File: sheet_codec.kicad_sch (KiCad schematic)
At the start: 20 parts, among them J3 Carrier LEFT 1-7, J4 Carrier RIGHT 1-7, U1 ES8389, U2 TPS7A2033

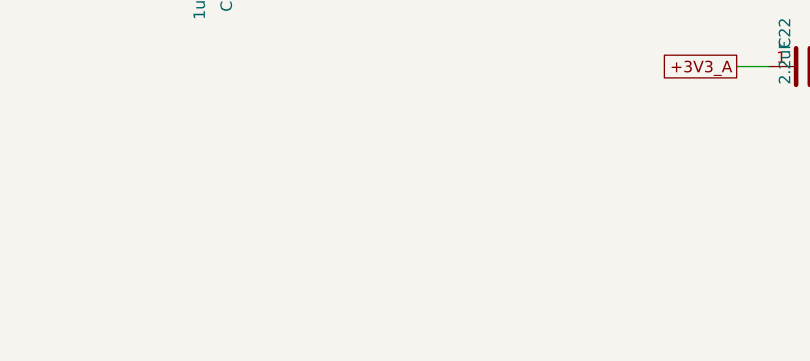
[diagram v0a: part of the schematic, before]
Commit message: codec: add J6 4-pin I2C header (3V3/AGND/SDA/SCL) for external display
- New scramble_hat:Conn_01x04 symbol + J6 in sheet_codec, connected to
  +3V3/AGND/SDA/SCL; placed on F.Cu and routed.
- Pin order (AGND/+3V3/SCL/SDA) set to match the external display's
  wiring harness.
- Fab set intentionally NOT regenerated (more design changes pending).
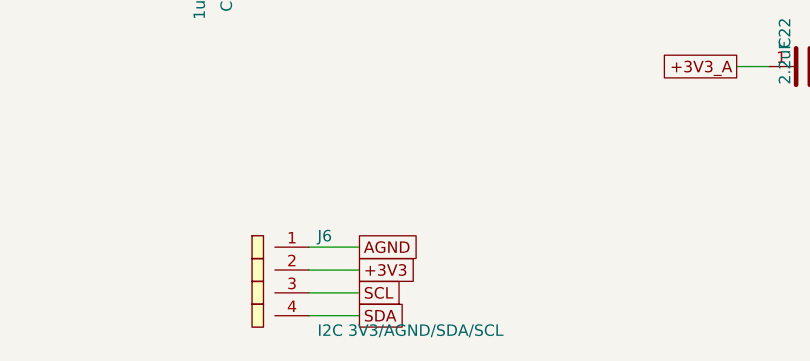
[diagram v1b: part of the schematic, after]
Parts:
- added J6: I2C 3V3/AGND/SDA/SCL, Connector_PinHeader_2.54mm:PinHeader_1x04_P2.54mm_Vertical, symbol scramble_hat:Conn_01x04
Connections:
- net +3V3: now also J6.2 (Pin_2)
- net AGND: now also J6.1 (Pin_1)
- net SCL: now also J6.3 (Pin_3)
- net SDA: now also J6.4 (Pin_4)
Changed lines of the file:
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@@
 	(wire
 		(pts
+			(xy 249.682 189.23) (xy 255.27 189.23)
+		)
+		(stroke
+			(width 0)
+			(type default)
+		)
+	)
+	(wire
+		(pts
 			(xy 299.974 117.602) (xy 309.626 117.682)
 		)
@@
 	(wire
 		(pts
+			(xy 249.682 196.85) (xy 255.27 196.85)
+		)
+		(stroke
+			(width 0)
+			(type default)
+		)
+	)
+	(wire
+		(pts
 			(xy 285.088 126.314) (xy 280.924 126.238)
 		)
@@
 	(wire
 		(pts
+			(xy 249.682 191.77) (xy 255.27 191.77)
+		)
+		(stroke
+			(width 0)
+			(type default)
+		)
+	)
+	(wire
+		(pts
 			(xy 285.088 123.774) (xy 280.924 123.698)
 		)
@@
 	(wire
 		(pts
+			(xy 249.682 194.31) (xy 255.27 194.31)
+		)
+		(stroke
+			(width 0)
+			(type default)
+		)
+	)
+	(wire
+		(pts
 			(xy 249.274 128.854) (xy 260.604 128.778)
 		)
@@
 		)
 	)
+	(global_label "SCL"
+		(shape passive)
+		(at 255.27 194.31 0)
+		(effects
+			(font
+				(size 1.27 1.27)
+			)
+			(justify left)
+		)
+		(property "Intersheetrefs" "${INTERSHEET_REFS}"
+			(at 255.27 194.31 0)
+			(hide yes)
+			(show_name no)
+			(do_not_autoplace no)
+			(effects
+				(font
+					(size 1.27 1.27)
+				)
+			)
+		)
+	)
 	(global_label "+3V3"
 		(shape passive)
@@
 		)
 	)
+	(global_label "+3V3"
+		(shape passive)
+		(at 255.27 191.77 0)
+		(effects
+			(font
+				(size 1.27 1.27)
+			)
+			(justify left)
+		)
+		(property "Intersheetrefs" "${INTERSHEET_REFS}"
+			(at 255.27 191.77 0)
+			(hide yes)
+			(show_name no)
+			(do_not_autoplace no)
+			(effects
+				(font
+					(size 1.27 1.27)
+				)
+			)
+		)
+	)
 	(global_label "+5V"
 		(shape passive)
@@
 		)
 	)
+	(global_label "SDA"
+		(shape passive)
+		(at 255.27 196.85 0)
+		(effects
+			(font
+				(size 1.27 1.27)
+			)
+			(justify left)
+		)
+		(property "Intersheetrefs" "${INTERSHEET_REFS}"
+			(at 255.27 196.85 0)
+			(hide yes)
+			(show_name no)
+			(do_not_autoplace no)
+			(effects
+				(font
+					(size 1.27 1.27)
+				)
+			)
+		)
+	)
 	(global_label "AGND"
 		(shape passive)
@@
 		)
 	)
+	(global_label "AGND"
+		(shape passive)
+		(at 255.27 189.23 0)
+		(effects
+			(font
+				(size 1.27 1.27)
+			)
+			(justify left)
+		)
+		(property "Intersheetrefs" "${INTERSHEET_REFS}"
+			(at 255.27 189.23 0)
+			(hide yes)
+			(show_name no)
+			(do_not_autoplace no)
+			(effects
+				(font
+					(size 1.27 1.27)
+				)
+			)
+		)
+	)
 	(global_label "+3V3"
 		(shape passive)
@@
 					(unit 1)
 				)
+			)
+		)
+	)
+	(symbol
+		(lib_id "scramble_hat:Conn_01x04")
+		(at 244.602 190.5 0)
+		(unit 1)
+		(body_style 1)
+		(exclude_from_sim no)
+		(in_bom yes)
+		(on_board yes)
+		(in_pos_files yes)
+		(dnp no)
+		(property "Reference" "J6"
+			(at 250.602 188 0)
+			(show_name no)
+			(do_not_autoplace no)
+			(effects
+				(font
+					(size 1.27 1.27)
+				)
+				(justify left)
+			)
+		)
+		(property "Value" "I2C 3V3/AGND/SDA/SCL"
+			(at 250.602 198.5 0)
+			(show_name no)
+			(do_not_autoplace no)
+			(effects
+				(font
+					(size 1.27 1.27)
+				)
+				(justify left)
+			)
+		)
+		(property "Footprint" "Connector_PinHeader_2.54mm:PinHeader_1x04_P2.54mm_Vertical"
+			(at 244.602 190.5 0)
+			(hide yes)
+			(show_name no)
+			(do_not_autoplace no)
+			(effects
+				(font
+					(size 1.27 1.27)
+				)
+			)
+		)
+		(property "Datasheet" ""
+			(at 244.602 190.5 0)
+			(hide yes)
+			(show_name no)
+			(do_not_autoplace no)
+			(effects
+				(font
+					(size 1.27 1.27)
+				)
+			)
+		)
+		(property "Description" ""
+			(at 244.602 190.5 0)
+			(hide yes)
+			(show_name no)
+			(do_not_autoplace no)
+			(effects
+				(font
+					(size 1.27 1.27)
+				)
+			)
+		)
+		(pin "1"
+		)
+		(pin "2"
+		)
+		(pin "3"
+		)
+		(pin "4"
+		)
+		(instances
+			(project "scramble_hat"
+				(path "/2b93e89d-bdf9-4578-8fa1-59d0c819a910/497e70f2-e060-4d80-87fd-d674c24dd8d4"
+					(reference "J6")
+					(unit 1)
+				)

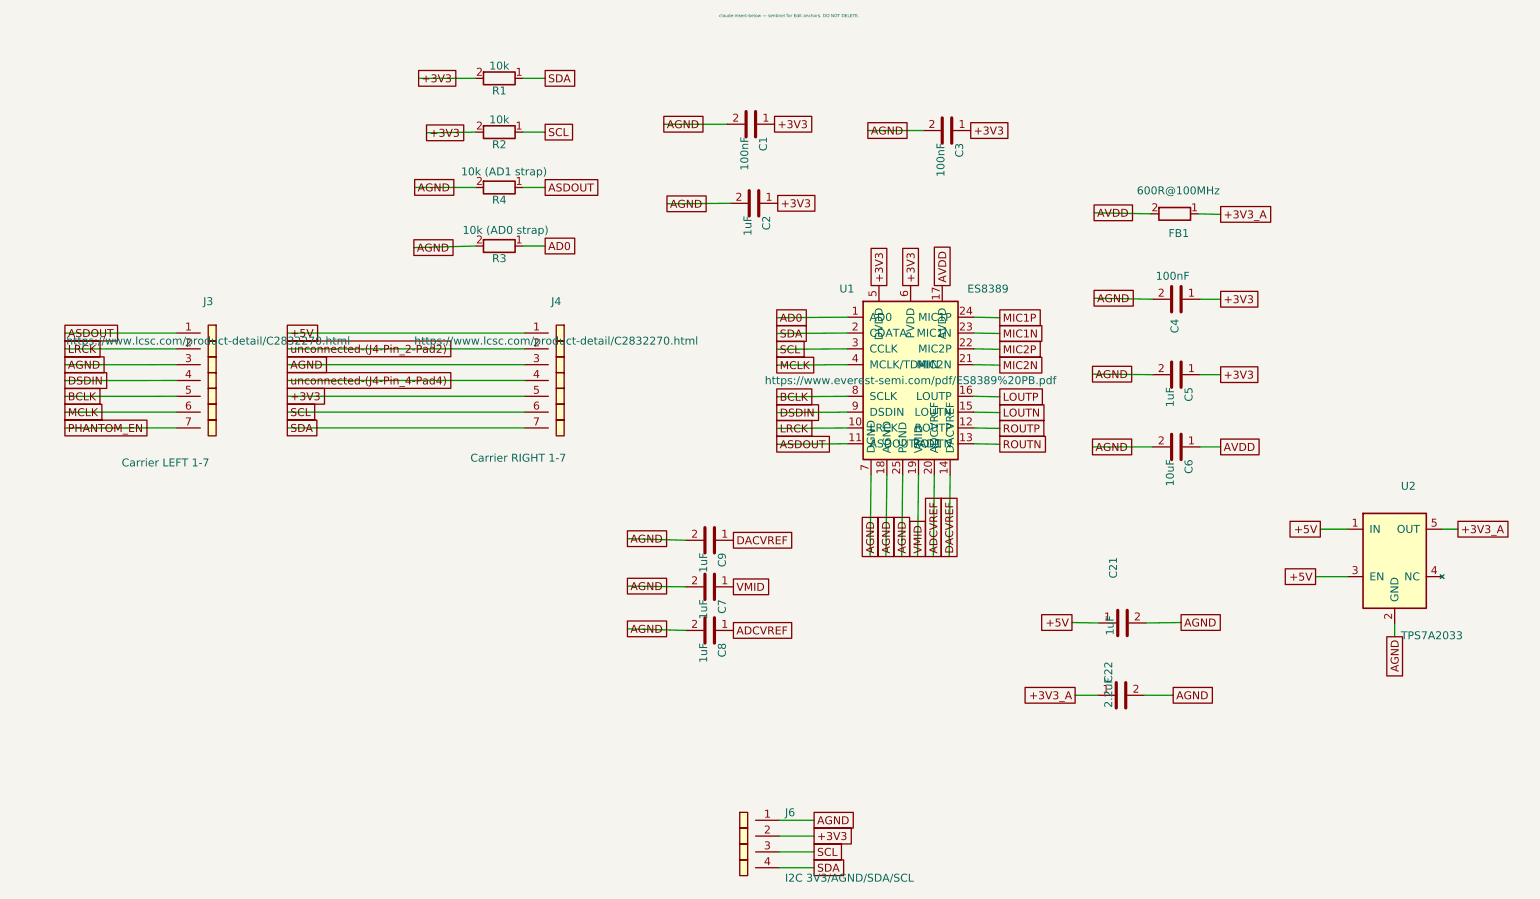
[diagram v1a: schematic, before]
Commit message: sch: add datasheet links, hide Datasheet/Description fields, remove sentinel text
- Filled 38 empty component Datasheet fields with LCSC product-page links (derived from the BOM part numbers); fixed D8's stale link (Kingbright KP-2012EC -> white KT-0805W / C34499). Existing manufacturer/distributor links kept.
- Hid the Datasheet and Description fields on all 53 placed components (most were previously shown, cluttering the canvas).
- Removed the 4 leftover sentinel text annotations.
- Netlist unchanged (check_sync: in sync, 53 comps / 46 nets).
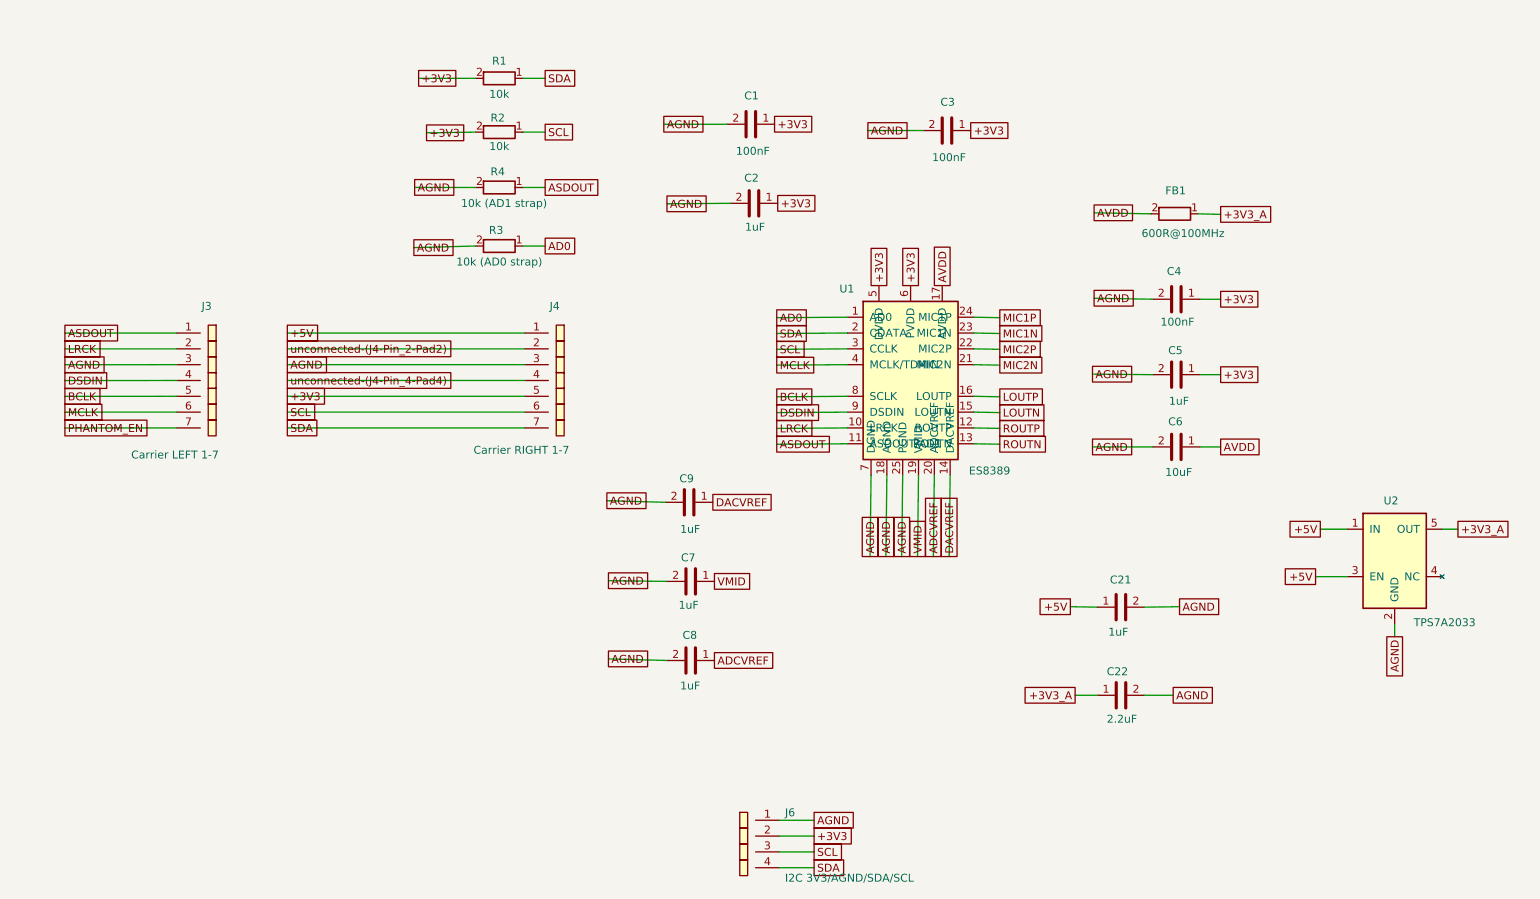
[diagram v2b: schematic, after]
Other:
- note removed: "claude-insert-below — sentinel for Edit anchors. DO NOT DELETE."
- moved on the sheet: C21, C7, C8, C9

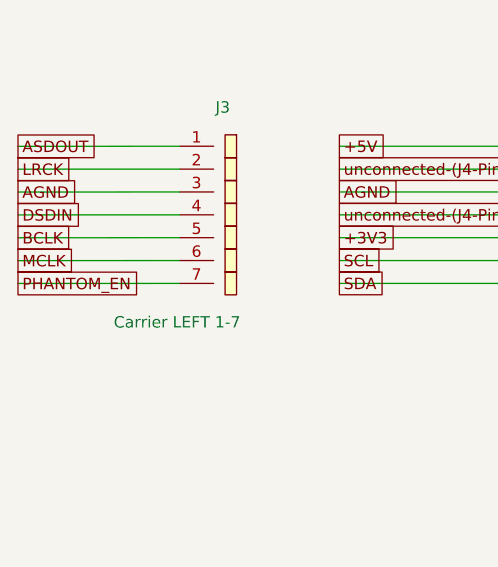
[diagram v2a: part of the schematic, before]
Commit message: feat: expose guitar plug-detect to the carrier on J3.7
Repurpose the dangling PHANTOM_EN line (vestigial since the manual SW1
pivot) as a firmware readback of the guitar-detect signal: J3.7 now
carries DET, so the carrier can see plug state (channel labeling,
muting the mode-switch click).

Instead of the planned 74HCT4053 swap -- no TSSOP-16 HCT4053 exists at
LCSC/JLCPCB from any vendor -- keep the in-stock 74HC4053 (C5648) and
run it from +3V3: VIH drops to 2.31V, so the 3.3V DET drives the select
pins in spec, and the line is native 3.3V for the ESP32-P4's
non-5V-tolerant GPIO. Analog range 0-3.3V covers the codec-bias-centred
signals (worst case ~0.1-2.9V at guitar full-scale); Ron rises
~80->150R, negligible into the codec input.

sheet_input: R19 pull-up, U4 VDD and its decap C29 move +5V -> +3V3
  (U3 buffer stays on +5V for headroom; C25 isolates its bias).
sheet_codec: J3.7 PHANTOM_EN -> DET.
BOM: U4 note updated (part unchanged).

Firmware: configure the J3.7 GPIO as input; low = guitar plugged.
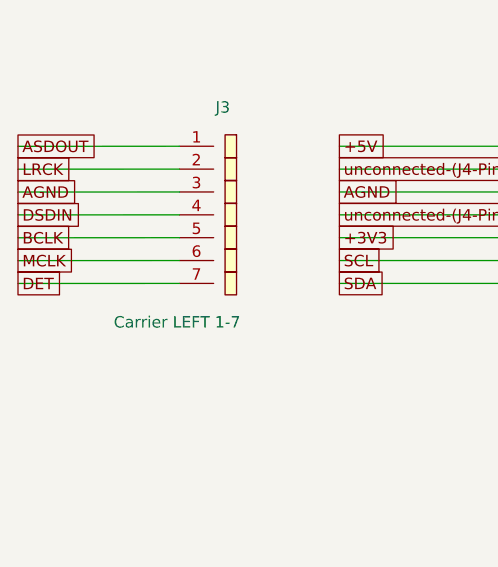
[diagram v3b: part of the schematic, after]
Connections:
- net PHANTOM_EN renamed DET
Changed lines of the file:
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@@
 		)
 	)
-	(global_label "PHANTOM_EN"
+	(global_label "DET"
 		(shape passive)
 		(at 134.978 126.248 0)
